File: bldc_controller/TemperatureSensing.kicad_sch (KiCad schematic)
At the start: 7 parts

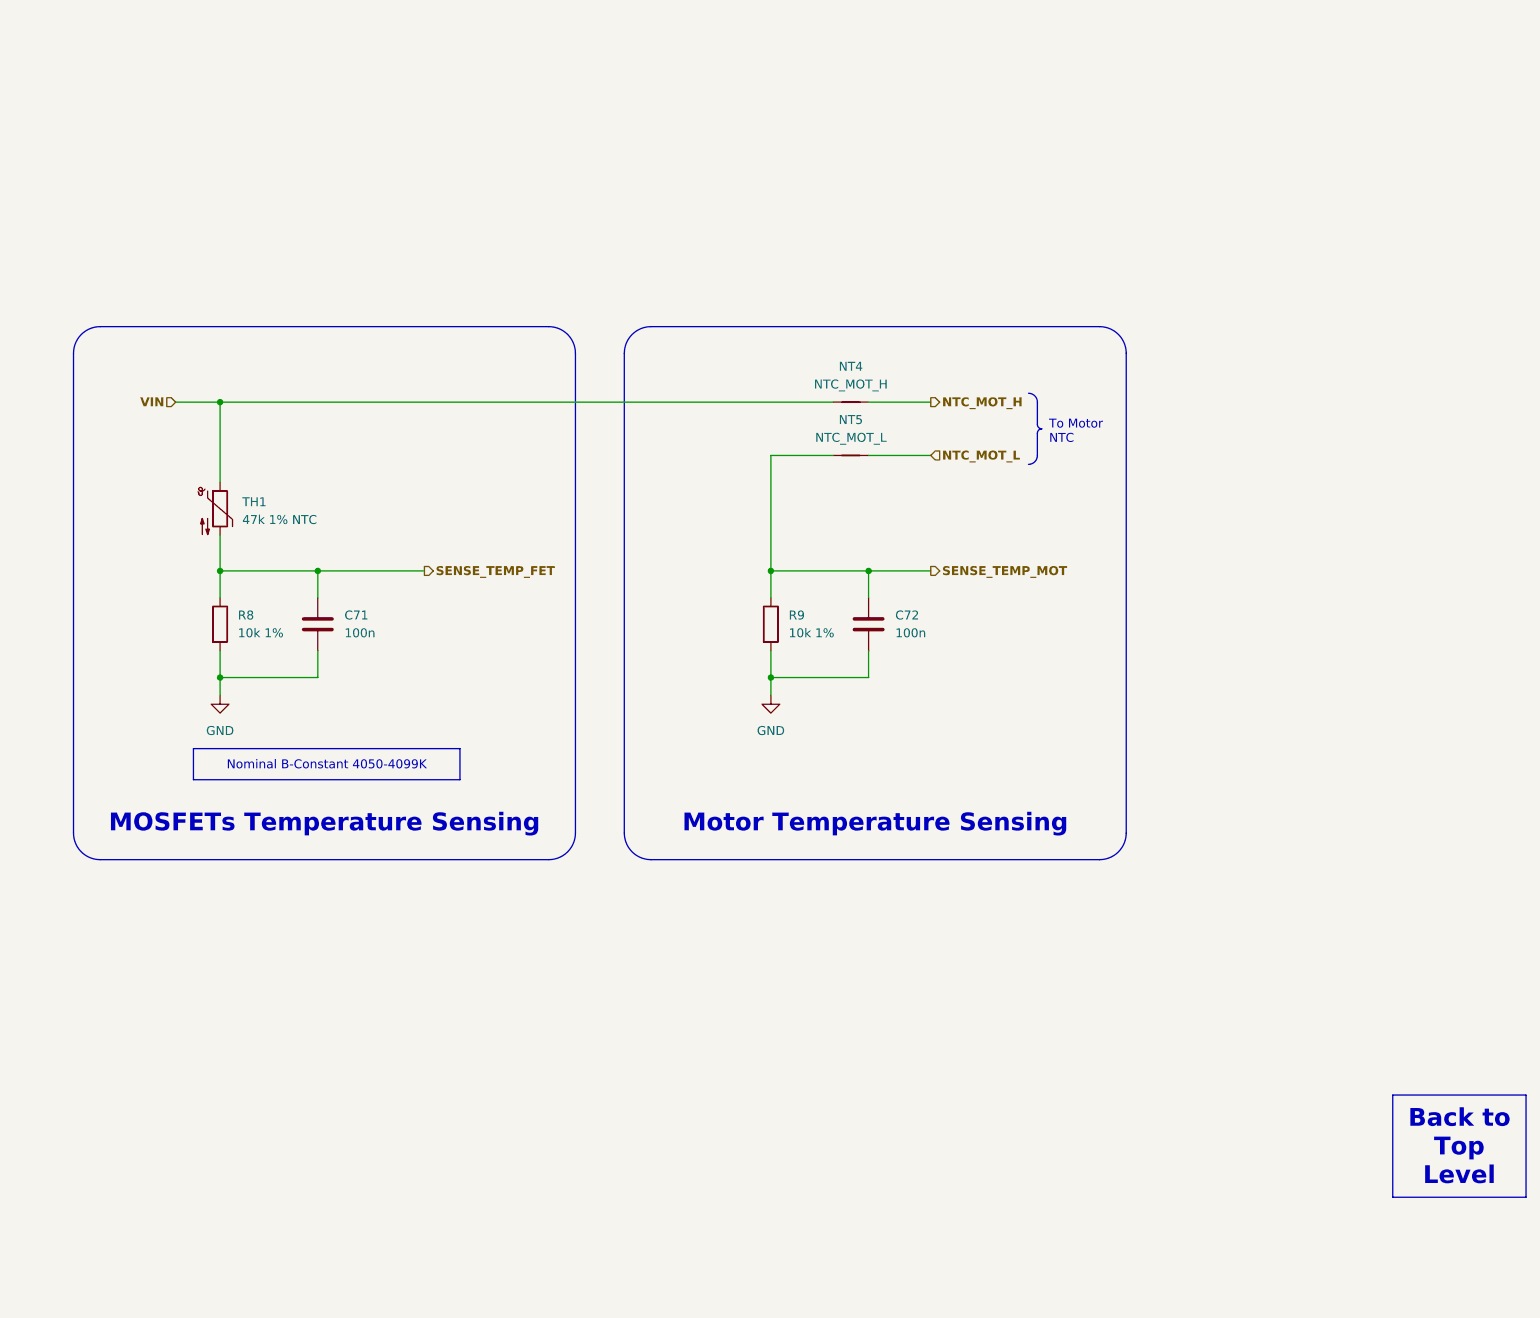
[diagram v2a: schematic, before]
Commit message: Added TVS diodes to all interfaces
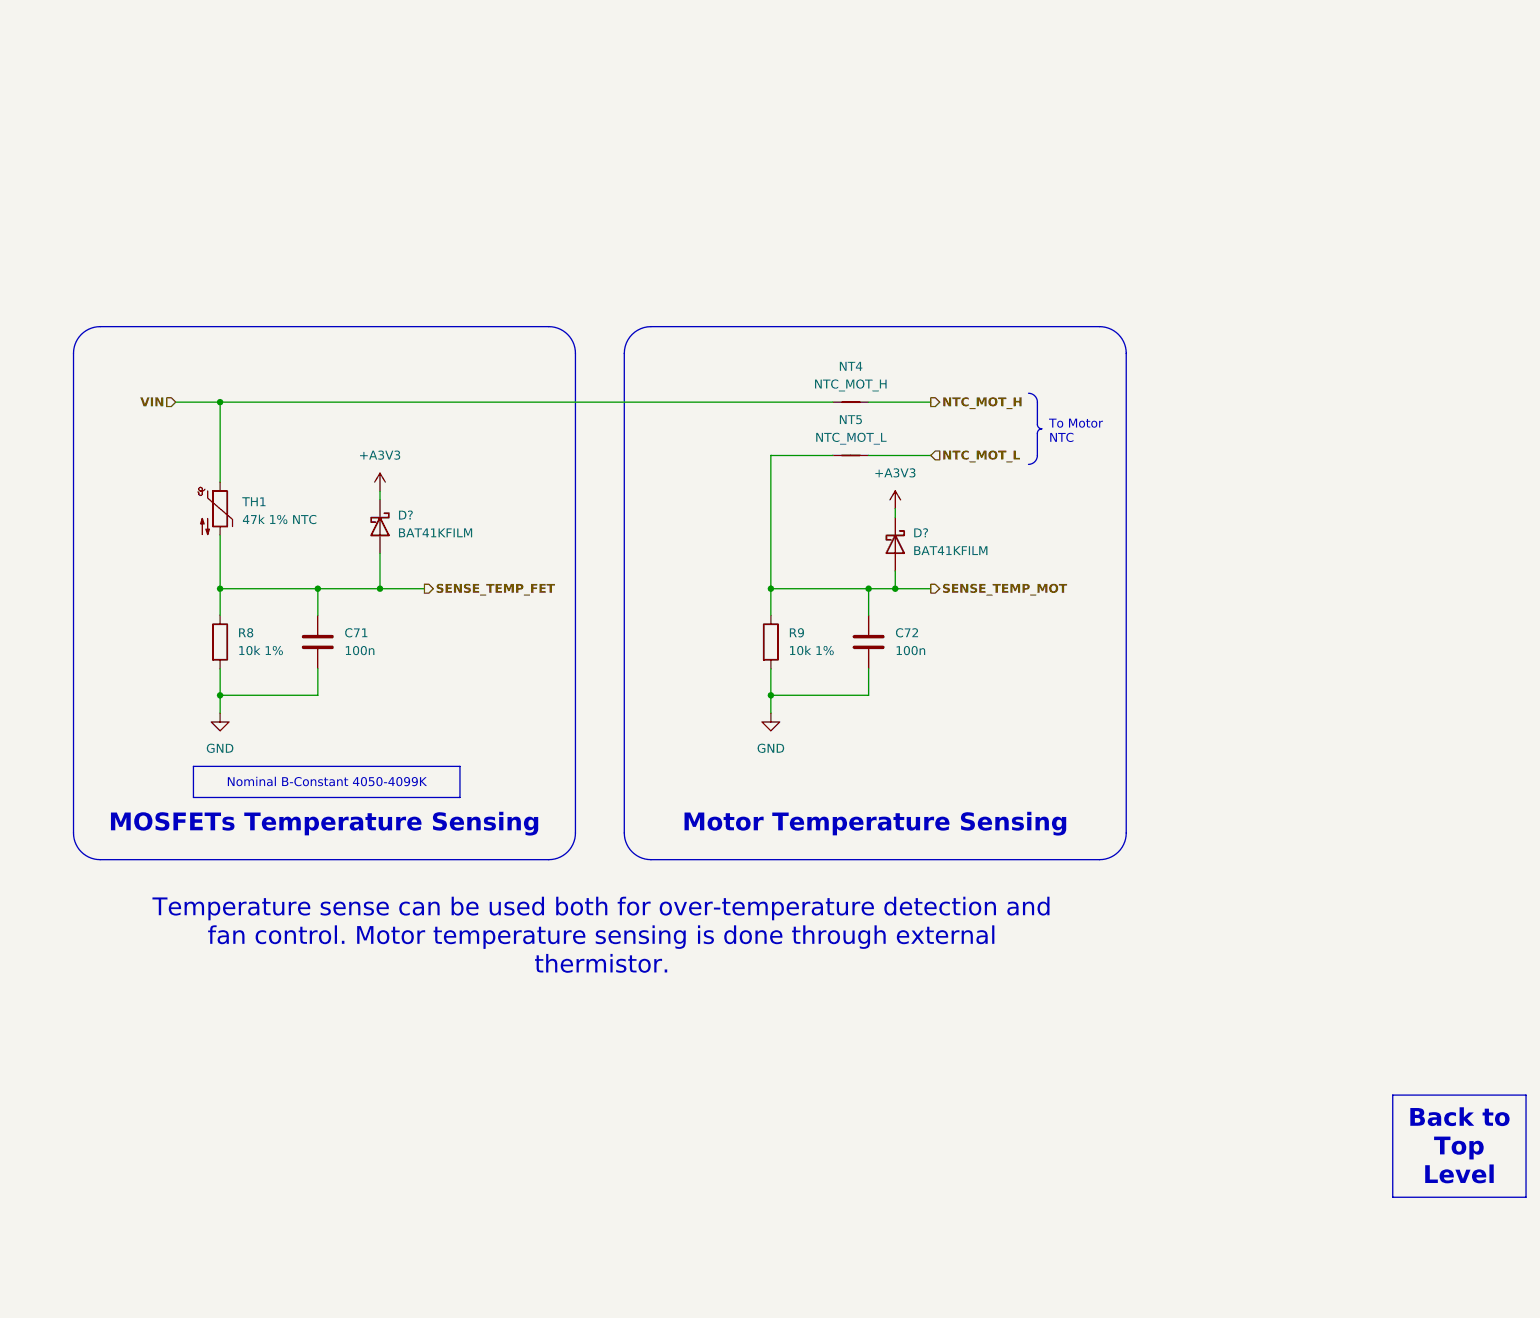
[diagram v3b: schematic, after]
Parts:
- added D? (x2): BAT41KFILM, Diode_SMD:D_SOD-523, symbol 0_diode:BAT41KFILM
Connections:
- net SENSE_TEMP_FET: now also D?.2 (A)
- net SENSE_TEMP_MOT: now also D?.2 (A)
- new net +A3V3: D?.1 (K), D?.1 (K)
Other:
- moved on the sheet: C71, C72, R8, R9

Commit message: might have fixed net issue, added dxf and svgs
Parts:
- gave numbers to parts that had none: 2
